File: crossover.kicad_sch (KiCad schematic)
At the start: 7 parts, among them J5 in_aux, U1 TL082

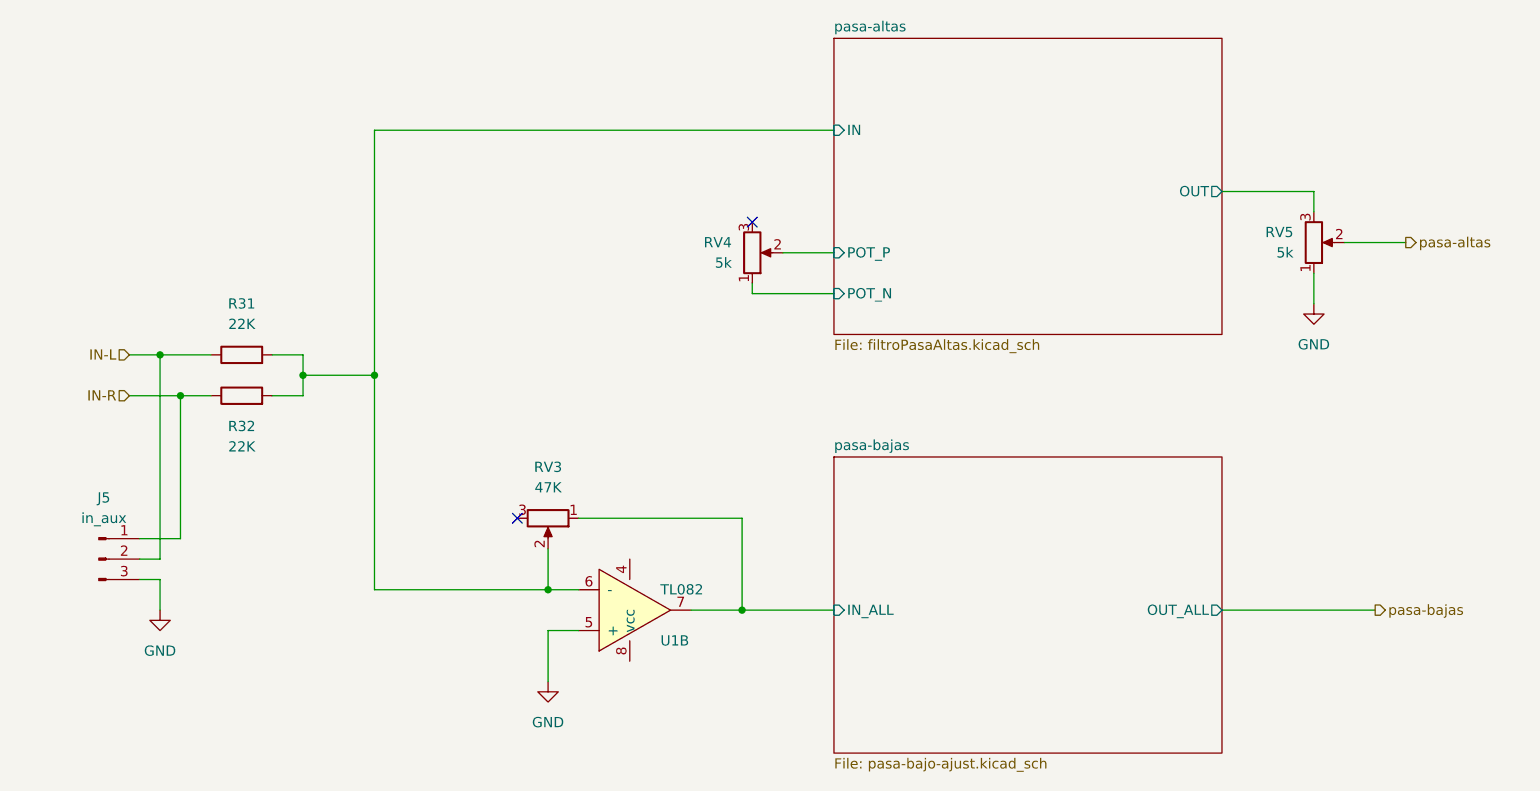
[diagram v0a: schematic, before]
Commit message: Separando las altas con resistencias de 22K
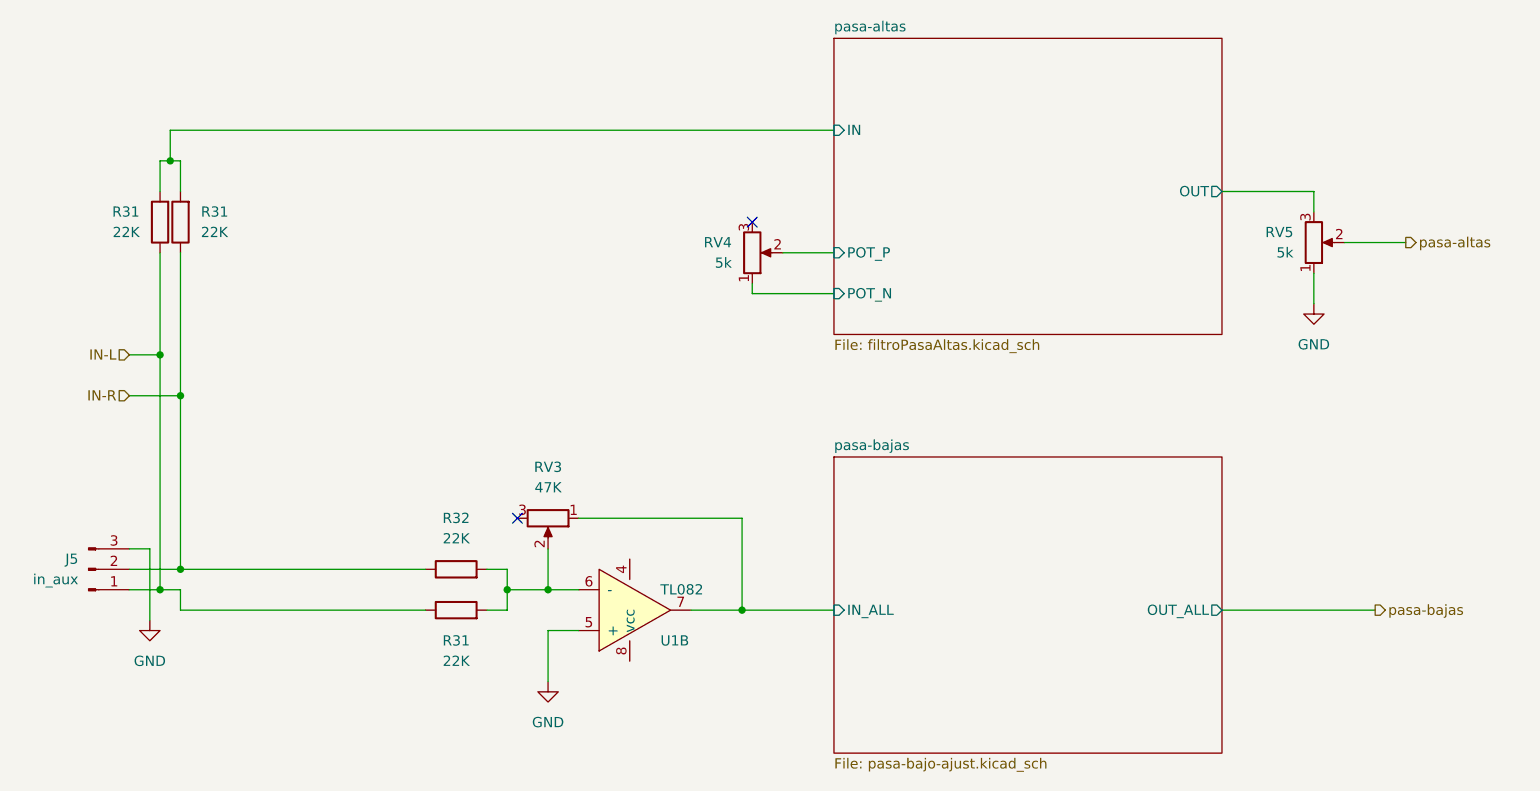
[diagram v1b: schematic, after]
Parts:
- added R31 (x2): 22K, Resistor_THT:R_Axial_DIN0207_L6.3mm_D2.5mm_P10.16mm_Horizontal, symbol Device:R
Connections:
- net IN-L: now also J5.1 (Pin_1), R31.1; no longer J5.2 (Pin_2)
- net IN-R: now also J5.2 (Pin_2), R31.1; no longer J5.1 (Pin_1)
- net pasa-altas/IN: now also R31.2, R31.2; no longer R31.2, R32.2, RV3.2, U1.6 (-)
- new net: R31.2, R32.2, RV3.2, U1.6 (-)
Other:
- moved on the sheet: J5, R31, R32

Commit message: actualizando a kicad 7
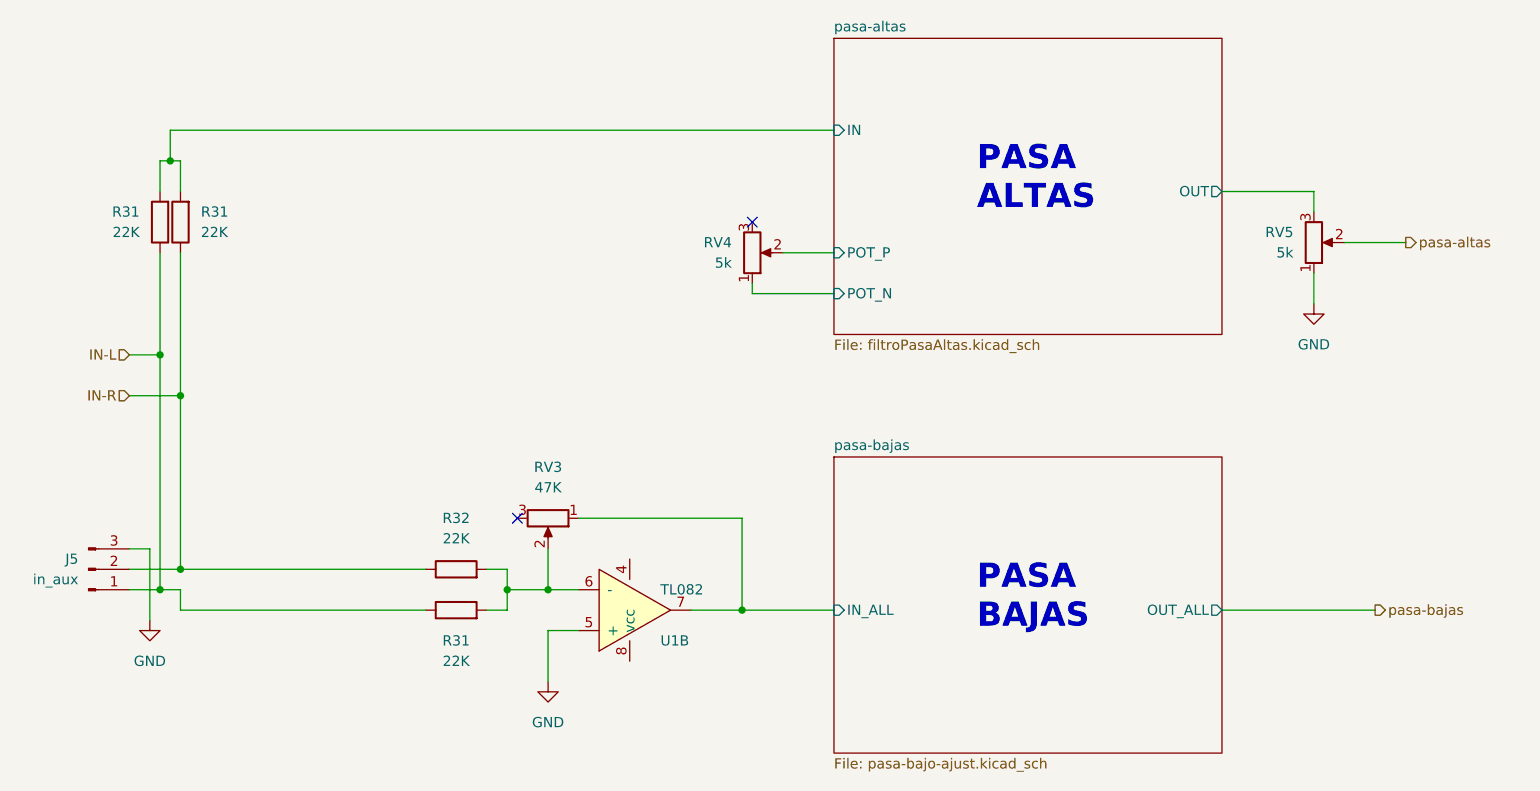
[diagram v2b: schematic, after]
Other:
- note added: "PASA ALTAS"
- note added: "PASA BAJAS"
- title: (none) -> AMPLIFICADOR ESTEREO 200, CONTROL DE TONOS
